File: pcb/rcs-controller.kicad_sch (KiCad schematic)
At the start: 0 parts

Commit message: Updated with footprint and more fleshed out circuit
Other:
- title: (none) -> RCS Controller Board

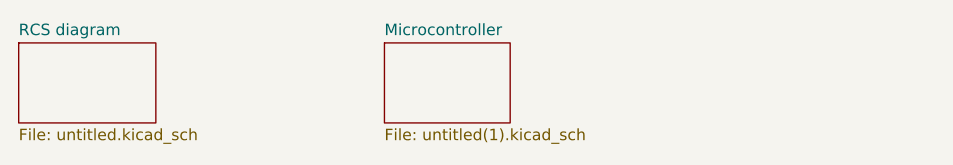
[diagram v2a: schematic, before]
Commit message: remove temporary and lock files that were somehow committed; rename schematic files to something sane.
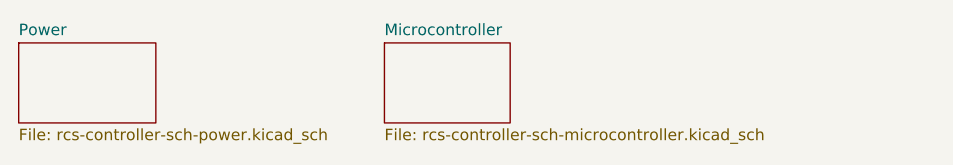
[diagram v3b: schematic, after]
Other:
- sheet RCS diagram renamed Power
- sheet Microcontroller: file untitled(1).kicad_sch -> rcs-controller-sch-microcontroller.kicad_sch
- sheet Power: file untitled.kicad_sch -> rcs-controller-sch-power.kicad_sch
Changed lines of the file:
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@@
 			(color 0 0 0 0.0000)
 		)
-		(property "Sheetname" "RCS diagram"
+		(property "Sheetname" "Power"
 			(at 31.75 53.8984 0)
 			(effects
@@
 			)
 		)
-		(property "Sheetfile" "untitled.kicad_sch"
+		(property "Sheetfile" "rcs-controller-sch-power.kicad_sch"
 			(at 31.75 64.0846 0)
 			(effects
@@
 			)
 		)
-		(property "Sheetfile" "untitled(1).kicad_sch"
+		(property "Sheetfile" "rcs-controller-sch-microcontroller.kicad_sch"
 			(at 72.39 64.0846 0)
 			(effects
@@
 			)
 		)
-		(property "Field2" ""
-			(at 72.39 54.61 0)
-			(effects
-				(font
-					(size 1.27 1.27)
-				)
-			)
-		)
